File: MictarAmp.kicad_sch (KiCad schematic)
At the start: 12 parts, among them J1 AudioJack3, J2 AudioJack4, J3 AudioJack2, J4 AudioJack3, SW1 SW_Push_SPDT, SW2 SW_Push_SPDT, U1 LM386, U2 TP4056

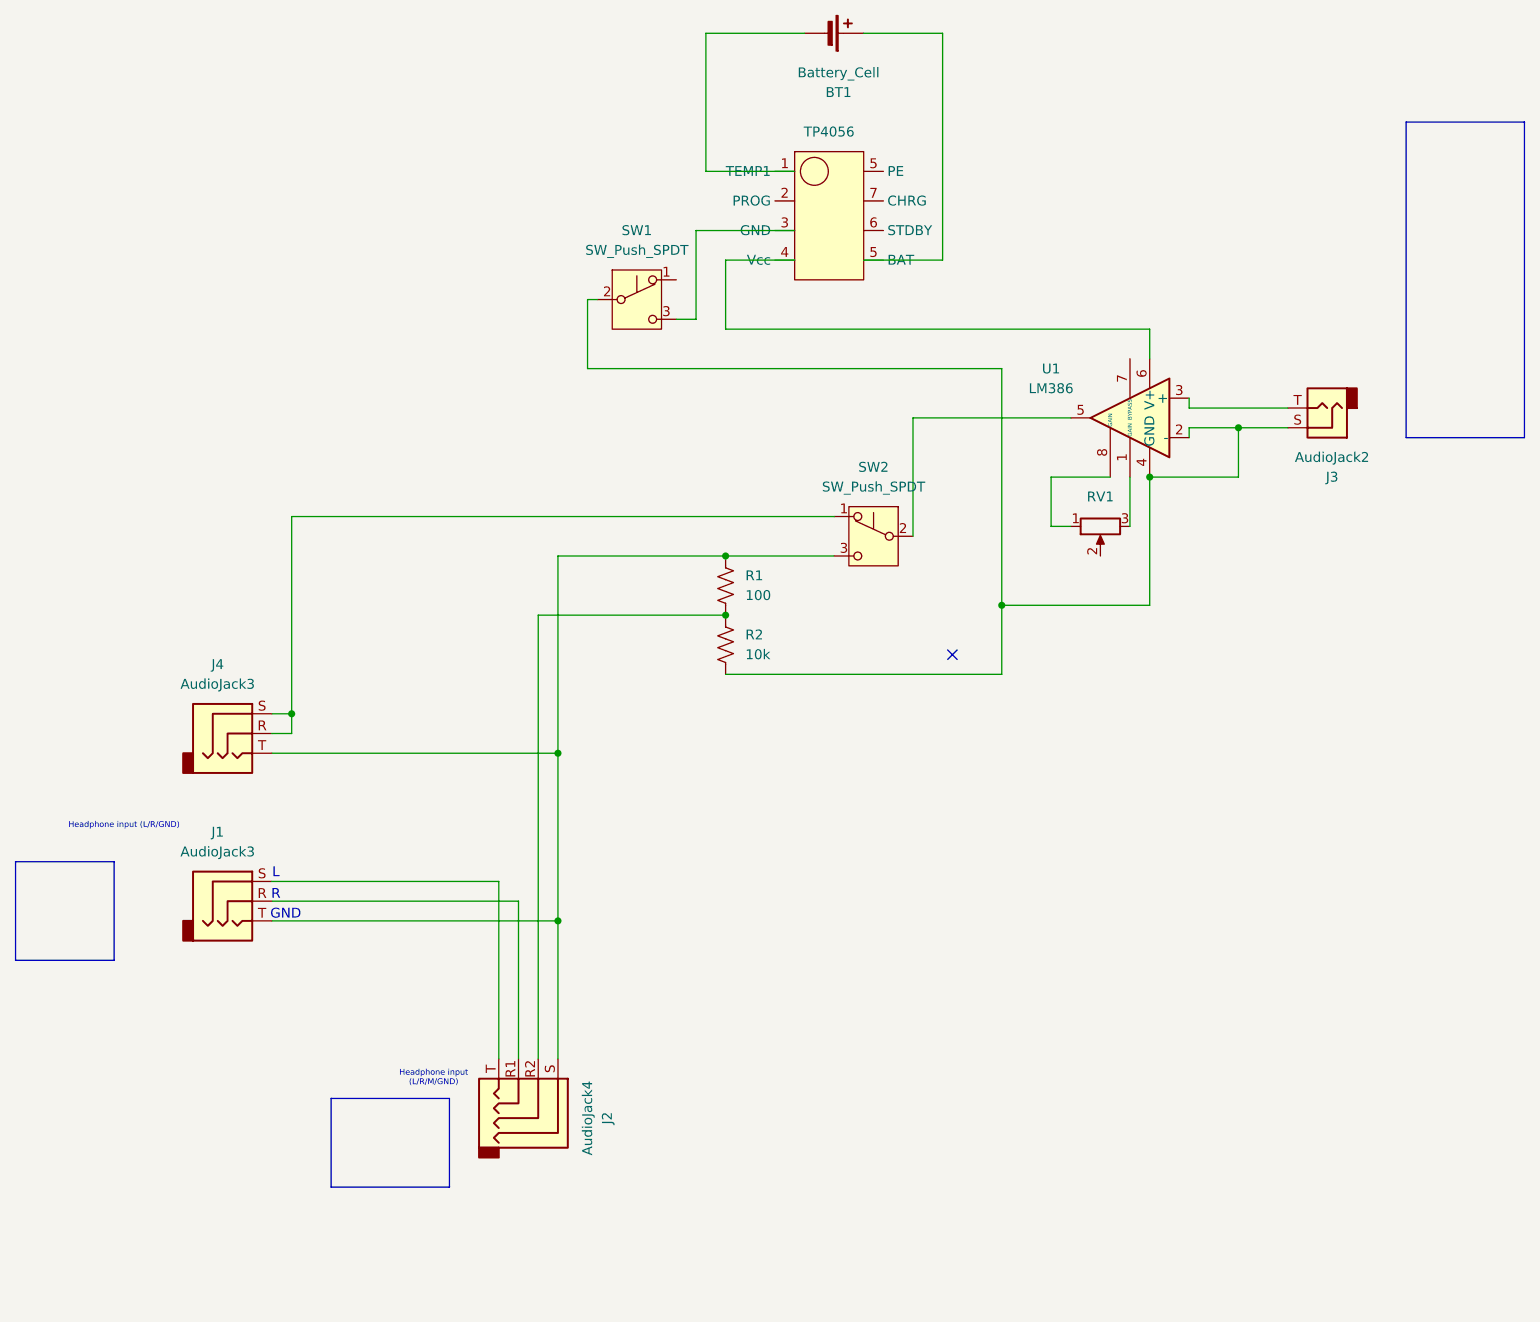
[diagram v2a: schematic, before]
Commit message: fixed incorrect audio jack wiring
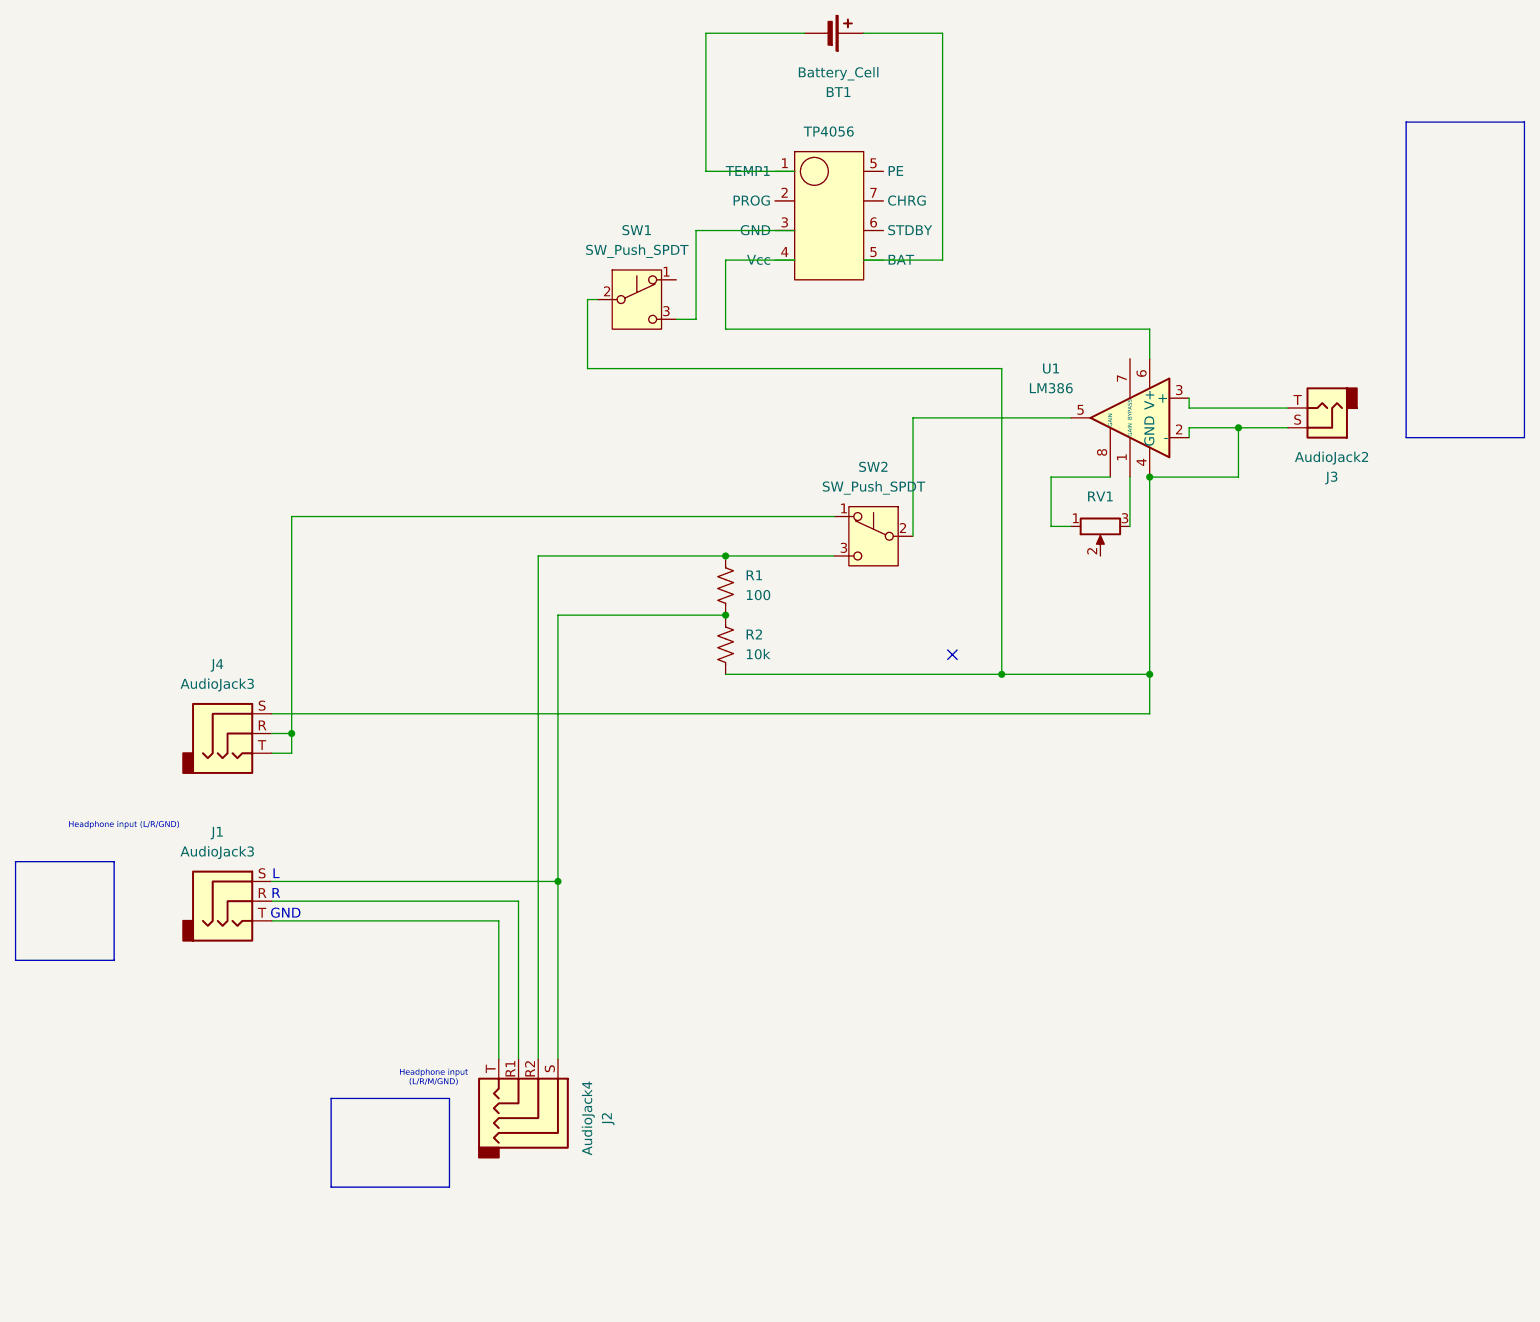
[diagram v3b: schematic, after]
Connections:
- net at J4.R, SW2.1 (A): now also J4.T; no longer J4.S
- net at J3.S, R2.1, SW1.2 (B)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: now also J4.S
- net at R1.1, R2.2: now also J1.S, J2.S; no longer J2.R2
- net at J2.T: now also J1.T; no longer J1.S
- new net: J2.R2, R1.2, SW2.3 (C)
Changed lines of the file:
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@@
 	(paper "A4")
 	(junction
-		(at 129.54 120.65)
+		(at 217.17 78.74)
 		(diameter 0)
 		(color 0 0 0 0)
 	)
 	(junction
-		(at 217.17 78.74)
+		(at 129.54 137.16)
 		(diameter 0)
 		(color 0 0 0 0)
 	)
 	(junction
-		(at 186.69 101.6)
+		(at 186.69 110.49)
 		(diameter 0)
 		(color 0 0 0 0)
 	)
 	(junction
-		(at 129.54 142.24)
+		(at 151.13 102.87)
 		(diameter 0)
 		(color 0 0 0 0)
 	)
 	(junction
-		(at 151.13 102.87)
+		(at 151.13 95.25)
 		(diameter 0)
 		(color 0 0 0 0)
 	)
 	(junction
-		(at 95.25 115.57)
+		(at 205.74 110.49)
 		(diameter 0)
 		(color 0 0 0 0)
 	)
 	(junction
-		(at 151.13 95.25)
+		(at 205.74 85.09)
 		(diameter 0)
 		(color 0 0 0 0)
 	)
 	(junction
-		(at 205.74 85.09)
+		(at 95.25 118.11)
 		(diameter 0)
 		(color 0 0 0 0)
@@
 	(wire
 		(pts
-			(xy 92.71 120.65) (xy 129.54 120.65)
+			(xy 205.74 85.09) (xy 205.74 110.49)
+		)
+		(stroke
+			(width 0)
+			(type default)
+		)
+	)
+	(wire
+		(pts
+			(xy 121.92 142.24) (xy 121.92 160.02)
 		)
 		(stroke
@@
 	(wire
 		(pts
-			(xy 193.04 91.44) (xy 195.58 91.44)
+			(xy 95.25 118.11) (xy 95.25 120.65)
 		)
 		(stroke
@@
 	(wire
 		(pts
-			(xy 210.82 76.2) (xy 223.52 76.2)
+			(xy 127 95.25) (xy 127 160.02)
 		)
 		(stroke
@@
 	(wire
 		(pts
-			(xy 148.59 27.94) (xy 148.59 45.72)
+			(xy 193.04 91.44) (xy 195.58 91.44)
 		)
 		(stroke
@@
 	(wire
 		(pts
-			(xy 92.71 142.24) (xy 129.54 142.24)
+			(xy 210.82 76.2) (xy 223.52 76.2)
 		)
 		(stroke
@@
 	(wire
 		(pts
-			(xy 133.35 71.12) (xy 133.35 62.23)
+			(xy 148.59 27.94) (xy 148.59 45.72)
 		)
 		(stroke
@@
 	(wire
 		(pts
-			(xy 179.07 27.94) (xy 179.07 57.15)
+			(xy 92.71 139.7) (xy 124.46 139.7)
 		)
 		(stroke
@@
 	(wire
 		(pts
-			(xy 203.2 85.09) (xy 203.2 91.44)
+			(xy 133.35 71.12) (xy 133.35 62.23)
 		)
 		(stroke
@@
 	(wire
 		(pts
-			(xy 151.13 66.04) (xy 205.74 66.04)
+			(xy 179.07 27.94) (xy 179.07 57.15)
 		)
 		(stroke
@@
 	(wire
 		(pts
-			(xy 121.92 137.16) (xy 121.92 160.02)
+			(xy 92.71 118.11) (xy 95.25 118.11)
 		)
 		(stroke
@@
 	(wire
 		(pts
-			(xy 161.29 27.94) (xy 148.59 27.94)
+			(xy 203.2 85.09) (xy 203.2 91.44)
 		)
 		(stroke
@@
 	(wire
 		(pts
-			(xy 151.13 95.25) (xy 129.54 95.25)
+			(xy 151.13 66.04) (xy 205.74 66.04)
 		)
 		(stroke
@@
 	(wire
 		(pts
-			(xy 92.71 139.7) (xy 124.46 139.7)
+			(xy 151.13 102.87) (xy 129.54 102.87)
 		)
 		(stroke
@@
 	(wire
 		(pts
-			(xy 148.59 45.72) (xy 160.02 45.72)
+			(xy 161.29 27.94) (xy 148.59 27.94)
 		)
 		(stroke
@@
 	(wire
 		(pts
-			(xy 175.26 77.47) (xy 175.26 92.71)
+			(xy 95.25 90.17) (xy 95.25 118.11)
 		)
 		(stroke
@@
 	(wire
 		(pts
-			(xy 205.74 85.09) (xy 205.74 101.6)
+			(xy 148.59 45.72) (xy 160.02 45.72)
 		)
 		(stroke
@@
 	(wire
 		(pts
-			(xy 95.25 118.11) (xy 92.71 118.11)
+			(xy 175.26 77.47) (xy 175.26 92.71)
 		)
 		(stroke
@@
 	(wire
 		(pts
-			(xy 217.17 78.74) (xy 217.17 85.09)
+			(xy 205.74 115.57) (xy 92.71 115.57)
 		)
 		(stroke
@@
 	(wire
 		(pts
-			(xy 147.32 53.34) (xy 160.02 53.34)
+			(xy 92.71 142.24) (xy 121.92 142.24)
 		)
 		(stroke
@@
 	(wire
 		(pts
-			(xy 193.04 85.09) (xy 193.04 91.44)
+			(xy 217.17 78.74) (xy 217.17 85.09)
 		)
 		(stroke
@@
 	(wire
 		(pts
-			(xy 186.69 101.6) (xy 186.69 110.49)
+			(xy 147.32 53.34) (xy 160.02 53.34)
 		)
 		(stroke
@@
 	(wire
 		(pts
-			(xy 144.78 64.77) (xy 147.32 64.77)
+			(xy 205.74 110.49) (xy 205.74 115.57)
 		)
 		(stroke
@@
 	(wire
 		(pts
-			(xy 129.54 95.25) (xy 129.54 120.65)
+			(xy 193.04 85.09) (xy 193.04 91.44)
 		)
 		(stroke
@@
 	(wire
 		(pts
-			(xy 129.54 142.24) (xy 129.54 160.02)
+			(xy 144.78 64.77) (xy 147.32 64.77)
 		)
 		(stroke
@@
 	(wire
 		(pts
-			(xy 147.32 64.77) (xy 147.32 53.34)
+			(xy 205.74 110.49) (xy 186.69 110.49)
 		)
 		(stroke
@@
 	(wire
 		(pts
-			(xy 200.66 85.09) (xy 193.04 85.09)
+			(xy 147.32 64.77) (xy 147.32 53.34)
 		)
 		(stroke
@@
 	(wire
 		(pts
-			(xy 179.07 57.15) (xy 168.91 57.15)
+			(xy 200.66 85.09) (xy 193.04 85.09)
 		)
 		(stroke
@@
 	(wire
 		(pts
-			(xy 151.13 102.87) (xy 127 102.87)
+			(xy 179.07 57.15) (xy 168.91 57.15)
 		)
 		(stroke
@@
 	(wire
 		(pts
-			(xy 210.82 76.2) (xy 210.82 74.93)
+			(xy 124.46 139.7) (xy 124.46 160.02)
 		)
 		(stroke
@@
 	(wire
 		(pts
-			(xy 95.25 115.57) (xy 92.71 115.57)
+			(xy 210.82 76.2) (xy 210.82 74.93)
 		)
 		(stroke
@@
 	(wire
 		(pts
-			(xy 95.25 115.57) (xy 95.25 118.11)
+			(xy 129.54 137.16) (xy 129.54 160.02)
 		)
 		(stroke
@@
 	(wire
 		(pts
-			(xy 205.74 66.04) (xy 205.74 69.85)
+			(xy 95.25 120.65) (xy 92.71 120.65)
 		)
 		(stroke
@@
 	(wire
 		(pts
-			(xy 133.35 62.23) (xy 134.62 62.23)
+			(xy 205.74 66.04) (xy 205.74 69.85)
 		)
 		(stroke
@@
 	(wire
 		(pts
-			(xy 210.82 78.74) (xy 217.17 78.74)
+			(xy 133.35 62.23) (xy 134.62 62.23)
 		)
 		(stroke
@@
 	(wire
 		(pts
-			(xy 160.02 57.15) (xy 151.13 57.15)
+			(xy 129.54 102.87) (xy 129.54 137.16)
 		)
 		(stroke
@@
 	(wire
 		(pts
-			(xy 129.54 120.65) (xy 129.54 142.24)
+			(xy 210.82 78.74) (xy 217.17 78.74)
 		)
 		(stroke
@@
 	(wire
 		(pts
-			(xy 165.1 95.25) (xy 151.13 95.25)
+			(xy 160.02 57.15) (xy 151.13 57.15)
 		)
 		(stroke
@@
 	(wire
 		(pts
-			(xy 92.71 137.16) (xy 121.92 137.16)
+			(xy 92.71 137.16) (xy 129.54 137.16)
 		)
 		(stroke
@@
 	(wire
 		(pts
-			(xy 186.69 101.6) (xy 205.74 101.6)
+			(xy 165.1 95.25) (xy 151.13 95.25)
 		)
 		(stroke
@@
 	(wire
 		(pts
-			(xy 186.69 101.6) (xy 186.69 71.12)
+			(xy 186.69 71.12) (xy 186.69 110.49)
 		)
 		(stroke
@@
 	(wire
 		(pts
-			(xy 127 102.87) (xy 127 160.02)
-		)
-		(stroke
-			(width 0)
-			(type default)
-		)
-	)
-	(wire
-		(pts
-			(xy 124.46 139.7) (xy 124.46 160.02)
-		)
-		(stroke
-			(width 0)
-			(type default)
-		)
-	)
-	(wire
-		(pts
-			(xy 95.25 90.17) (xy 95.25 115.57)
+			(xy 151.13 95.25) (xy 127 95.25)
 		)
 		(stroke
@@
 	(text "L"
 		(exclude_from_sim no)
-		(at 93.218 136.144 0)
+		(at 93.218 136.398 0)
 		(effects
 			(font
@@
 		)
 	)
-	(text "GND"
+	(text "GND\n"
 		(exclude_from_sim no)
 		(at 94.488 141.478 0)

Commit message: fixed incorrect audio jack wiring, again
also untied negative guitar input from ground
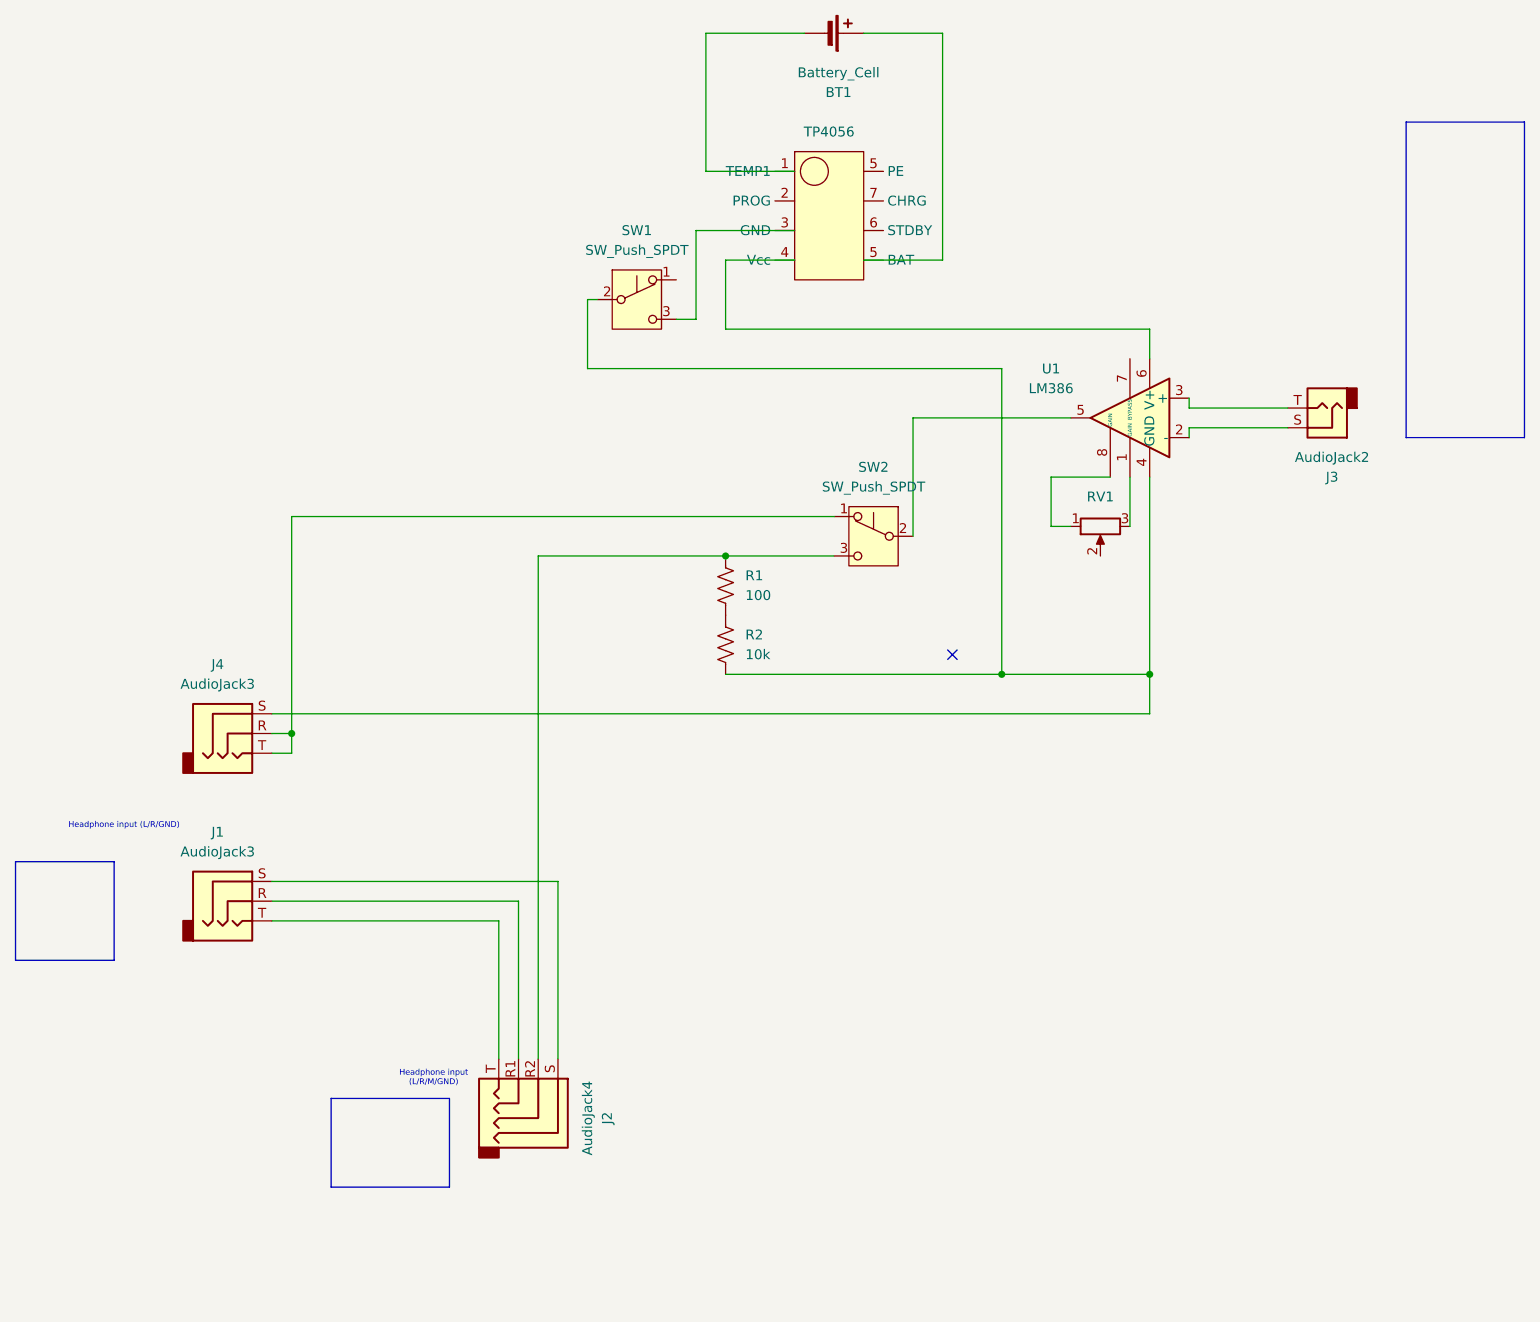
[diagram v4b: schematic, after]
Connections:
- net at J4.S, R2.1, SW1.2 (B)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: no longer J3.S, U1.2 (-)
- net at R1.1, R2.2: no longer J1.S, J2.S
- new net: J3.S, U1.2 (-)
- new net: J1.S, J2.S
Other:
- note removed: "GND"
- note removed: "L"
- note removed: "R"
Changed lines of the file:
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@@
 	(paper "A4")
 	(junction
-		(at 217.17 78.74)
-		(diameter 0)
-		(color 0 0 0 0)
-	)
-	(junction
-		(at 129.54 137.16)
-		(diameter 0)
-		(color 0 0 0 0)
-	)
-	(junction
 		(at 186.69 110.49)
 		(diameter 0)
@@
 	)
 	(junction
-		(at 151.13 102.87)
-		(diameter 0)
-		(color 0 0 0 0)
-	)
-	(junction
 		(at 151.13 95.25)
 		(diameter 0)
@@
 	)
 	(junction
-		(at 205.74 85.09)
-		(diameter 0)
-		(color 0 0 0 0)
-	)
-	(junction
 		(at 95.25 118.11)
 		(diameter 0)
@@
 	(wire
 		(pts
-			(xy 121.92 142.24) (xy 121.92 160.02)
-		)
-		(stroke
-			(width 0)
-			(type default)
-		)
-	)
-	(wire
-		(pts
-			(xy 217.17 85.09) (xy 205.74 85.09)
-		)
-		(stroke
-			(width 0)
-			(type default)
-		)
-	)
-	(wire
-		(pts
 			(xy 95.25 118.11) (xy 95.25 120.65)
 		)
@@
 	(wire
 		(pts
-			(xy 151.13 102.87) (xy 129.54 102.87)
-		)
-		(stroke
-			(width 0)
-			(type default)
-		)
-	)
-	(wire
-		(pts
 			(xy 161.29 27.94) (xy 148.59 27.94)
 		)
@@
 	(wire
 		(pts
-			(xy 168.91 27.94) (xy 179.07 27.94)
-		)
-		(stroke
-			(width 0)
-			(type default)
-		)
-	)
-	(wire
-		(pts
-			(xy 205.74 115.57) (xy 92.71 115.57)
+			(xy 129.54 137.16) (xy 129.54 160.02)
 		)
 		(stroke
@@
 	(wire
 		(pts
-			(xy 92.71 142.24) (xy 121.92 142.24)
+			(xy 168.91 27.94) (xy 179.07 27.94)
 		)
 		(stroke
@@
 	(wire
 		(pts
-			(xy 217.17 78.74) (xy 217.17 85.09)
+			(xy 205.74 115.57) (xy 92.71 115.57)
 		)
 		(stroke
@@
 	(wire
 		(pts
-			(xy 195.58 77.47) (xy 175.26 77.47)
+			(xy 92.71 142.24) (xy 121.92 142.24)
 		)
 		(stroke
@@
 	(wire
 		(pts
-			(xy 151.13 57.15) (xy 151.13 66.04)
+			(xy 195.58 77.47) (xy 175.26 77.47)
 		)
 		(stroke
@@
 	(wire
 		(pts
-			(xy 95.25 90.17) (xy 165.1 90.17)
+			(xy 151.13 57.15) (xy 151.13 66.04)
 		)
 		(stroke
@@
 	(wire
 		(pts
-			(xy 124.46 139.7) (xy 124.46 160.02)
+			(xy 95.25 90.17) (xy 165.1 90.17)
 		)
 		(stroke
@@
 	(wire
 		(pts
-			(xy 210.82 76.2) (xy 210.82 74.93)
+			(xy 124.46 139.7) (xy 124.46 160.02)
 		)
 		(stroke
@@
 	(wire
 		(pts
-			(xy 186.69 110.49) (xy 151.13 110.49)
+			(xy 210.82 76.2) (xy 210.82 74.93)
 		)
 		(stroke
@@
 	(wire
 		(pts
-			(xy 133.35 71.12) (xy 186.69 71.12)
+			(xy 186.69 110.49) (xy 151.13 110.49)
 		)
 		(stroke
@@
 	(wire
 		(pts
-			(xy 129.54 137.16) (xy 129.54 160.02)
+			(xy 133.35 71.12) (xy 186.69 71.12)
 		)
 		(stroke
@@
 	(wire
 		(pts
-			(xy 205.74 66.04) (xy 205.74 69.85)
+			(xy 121.92 142.24) (xy 121.92 160.02)
 		)
 		(stroke
@@
 	(wire
 		(pts
-			(xy 133.35 62.23) (xy 134.62 62.23)
+			(xy 205.74 66.04) (xy 205.74 69.85)
 		)
 		(stroke
@@
 	(wire
 		(pts
-			(xy 129.54 102.87) (xy 129.54 137.16)
+			(xy 133.35 62.23) (xy 134.62 62.23)
 		)
 		(stroke
@@
 	(wire
 		(pts
-			(xy 210.82 78.74) (xy 217.17 78.74)
+			(xy 210.82 78.74) (xy 223.52 78.74)
 		)
 		(stroke
@@
 	(wire
 		(pts
-			(xy 217.17 78.74) (xy 223.52 78.74)
-		)
-		(stroke
-			(width 0)
-			(type default)
-		)
-	)
-	(wire
-		(pts
 			(xy 151.13 95.25) (xy 127 95.25)
 		)
@@
 		)
 	)
-	(text "L"
-		(exclude_from_sim no)
-		(at 93.218 136.398 0)
-		(effects
-			(font
-				(size 1.27 1.27)
-			)
-		)
-	)
 	(text "Headphone input (L/R/GND)"
 		(exclude_from_sim no)
@@
 			)
 		)
-	)
-	(text "GND\n"
-		(exclude_from_sim no)
-		(at 94.488 141.478 0)
-		(effects
-			(font
-				(size 1.27 1.27)
-			)
-		)
-	)
-	(text "R"
-		(exclude_from_sim no)
-		(at 93.218 138.938 0)
-		(effects
-			(font
-				(size 1.27 1.27)
-			)
-		)
